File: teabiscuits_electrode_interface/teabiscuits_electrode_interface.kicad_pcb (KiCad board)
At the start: 2 copper layers, 34 x 89.6 mm, 18 parts, among them J1 Conn_Coaxial, J10 Conn_01x01, J2 Conn_Coaxial, J3 Conn_Coaxial, J4 Conn_Coaxial, J5 Conn_Coaxial, J6 Conn_Coaxial, J7 Conn_Coaxial, J8 Conn_Coaxial, J9 Conn_01x01

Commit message: Revised electrode interface (bigger holes) and power (connector was wrong way round)
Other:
- board text added: "Teabiscuits ElectrodeInt r2"
- board text removed: "Teabiscuits ElectrodeInt r1"

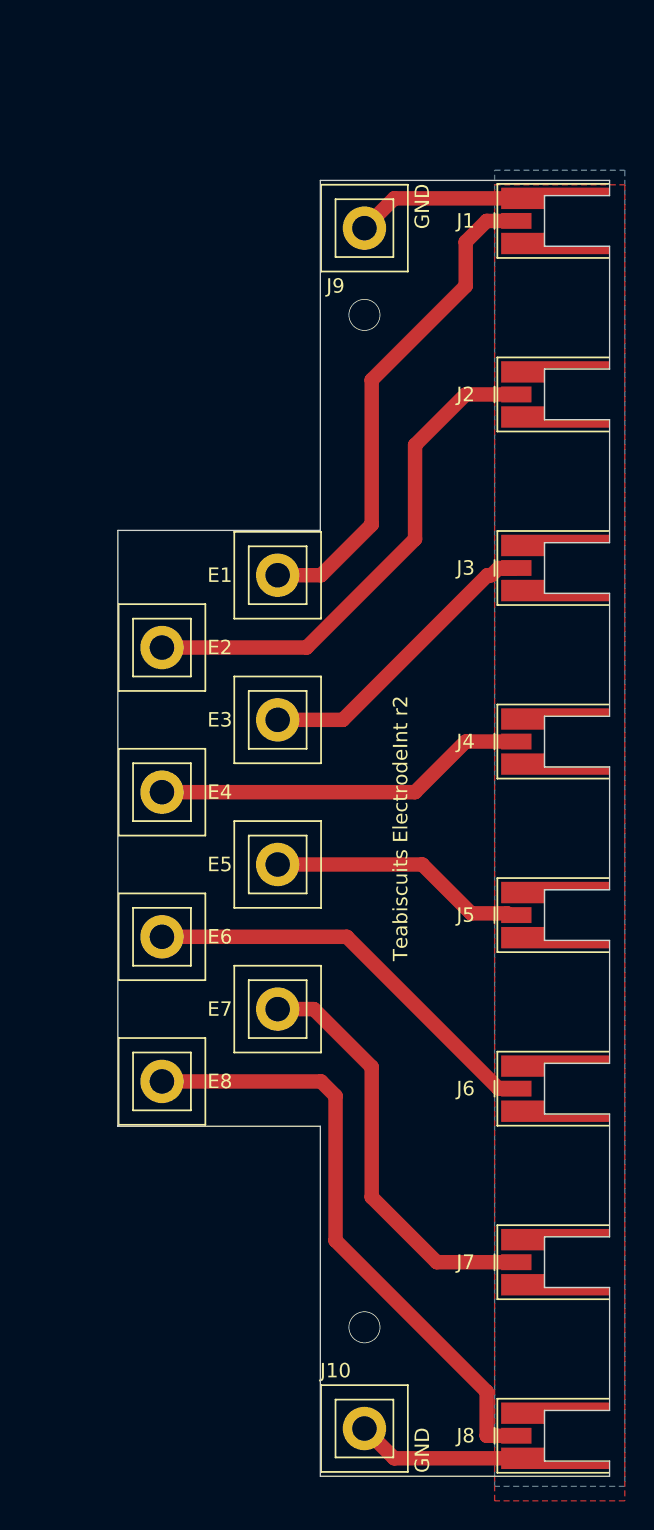
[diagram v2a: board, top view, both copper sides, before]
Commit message: Electrode interface (single channel version)
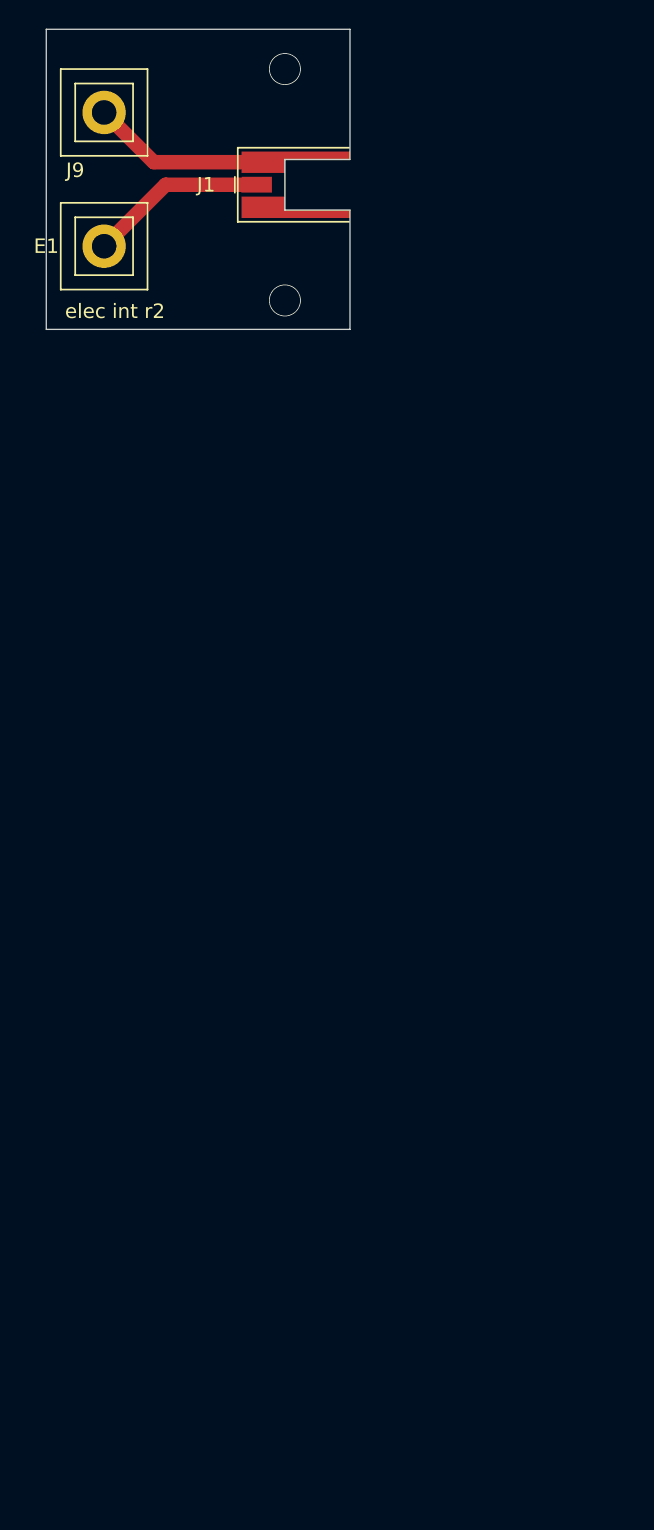
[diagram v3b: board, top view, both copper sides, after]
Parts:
- removed E2, E3, E4, E5, E6, E7, E8, J10: Conn_01x01, screwterminal:KeystonePost
- removed J2, J3, J4, J5, J6, J7, J8: Conn_Coaxial, Connector_Coaxial:MMCX_Molex_73415-0961_Horizontal_1.0mm-PCB
- moved E1 25.7 mm to (110.0, 46.2)
- moved J9 19.7 mm to (110.0, 37.0)
- moved J1 18.1 mm to (123.2, 42.0)
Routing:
- net Net-(E8-Pad1): track 42.3 -> 0.00 mm
- net Net-(E2-Pad1): track 35.6 -> 0.00 mm
- net Net-(E7-Pad1): track 29.0 -> 0.00 mm
- net Net-(E6-Pad1): track 28.8 -> 0.00 mm
- net Net-(E4-Pad1): track 25.9 -> 0.00 mm
- net Net-(E1-Pad1): track 34.3 -> 12.3 mm
- net Net-(E3-Pad1): track 20.8 -> 0.00 mm
- net Net-(E5-Pad1): track 17.9 -> 0.00 mm
- net GND: track 23.6 -> 12.4 mm
- removed copper zone on B.Cu, net GND
- removed copper zone on F.Cu, net GND
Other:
- board size 34 x 89.6 mm -> 21 x 20.8 mm
- board text added: "elec int r2"
- board text removed: "GND"
- board text removed: "Teabiscuits ElectrodeInt r2"
